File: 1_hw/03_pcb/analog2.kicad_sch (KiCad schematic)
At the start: 19 parts, among them U22 TPL0401B-10, U23 THS3491, U24 ADG1219BRJZ

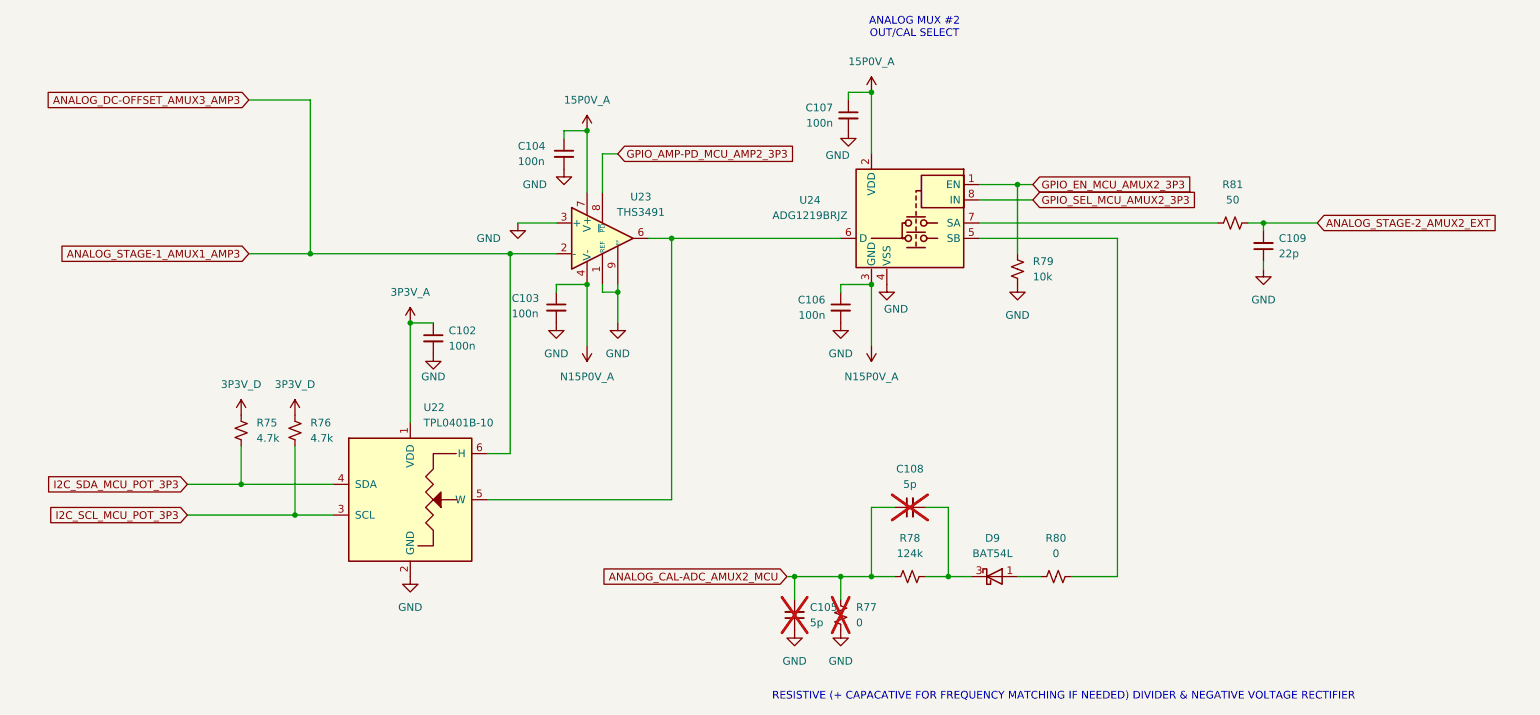
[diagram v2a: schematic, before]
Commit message: FEAT: Changed Inductor to higher current. Continued layout. Assigned some Netclasses.
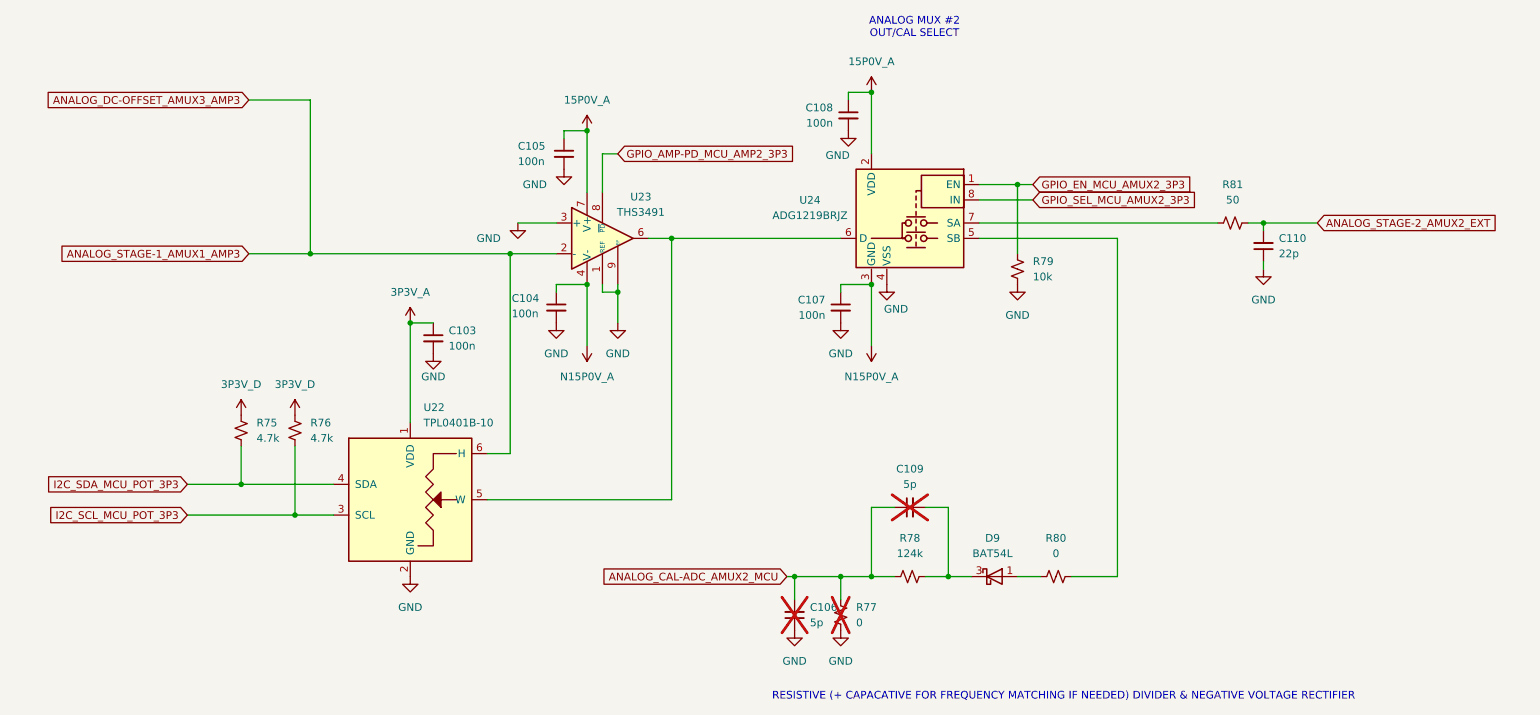
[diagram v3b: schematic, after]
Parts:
- renumbered C102 to C103, C103 to C104, C104 to C105, C105 to C106, C106 to C107, C107 to C108, C108 to C109, C109 to C110
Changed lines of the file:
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@@
 		(dnp no)
 		(fields_autoplaced yes)
-		(property "Reference" "#PWR0272"
+		(property "Reference" "#PWR0274"
 			(at 152.4 104.14 0)
 			(effects
@@
 			(project "arb"
 				(path "/866ef9be-3b01-4288-a6e0-a2357aa17e50/e46c6640-71a3-4b78-b602-0f6be9676e36"
-					(reference "#PWR0272")
+					(reference "#PWR0274")
 					(unit 1)
 				)
@@
 		(dnp no)
 		(fields_autoplaced yes)
-		(property "Reference" "#PWR0273"
+		(property "Reference" "#PWR0275"
 			(at 152.4 154.94 0)
 			(effects
@@
 			(project "arb"
 				(path "/866ef9be-3b01-4288-a6e0-a2357aa17e50/e46c6640-71a3-4b78-b602-0f6be9676e36"
-					(reference "#PWR0273")
+					(reference "#PWR0275")
 					(unit 1)
 				)
@@
 		(dnp no)
 		(fields_autoplaced yes)
-		(property "Reference" "#PWR0269"
+		(property "Reference" "#PWR0271"
 			(at 110.49 97.79 0)
 			(effects
@@
 			(project "arb"
 				(path "/866ef9be-3b01-4288-a6e0-a2357aa17e50/e46c6640-71a3-4b78-b602-0f6be9676e36"
-					(reference "#PWR0269")
+					(reference "#PWR0271")
 					(unit 1)
 				)
@@
 		(dnp no)
 		(fields_autoplaced yes)
-		(property "Reference" "C107"
+		(property "Reference" "C108"
 			(at 151.13 62.2363 0)
 			(effects
@@
 			(project "arb"
 				(path "/866ef9be-3b01-4288-a6e0-a2357aa17e50/e46c6640-71a3-4b78-b602-0f6be9676e36"
-					(reference "C107")
+					(reference "C108")
 					(unit 1)
 				)
@@
 		(dnp no)
 		(fields_autoplaced yes)
-		(property "Reference" "#PWR0271"
+		(property "Reference" "#PWR0273"
 			(at 144.78 154.94 0)
 			(effects
@@
 			(project "arb"
 				(path "/866ef9be-3b01-4288-a6e0-a2357aa17e50/e46c6640-71a3-4b78-b602-0f6be9676e36"
-					(reference "#PWR0271")
+					(reference "#PWR0273")
 					(unit 1)
 				)
@@
 		(on_board yes)
 		(dnp no)
-		(property "Reference" "#PWR0274"
+		(property "Reference" "#PWR0276"
 			(at 153.67 72.39 0)
 			(effects
@@
 			(project "arb"
 				(path "/866ef9be-3b01-4288-a6e0-a2357aa17e50/e46c6640-71a3-4b78-b602-0f6be9676e36"
-					(reference "#PWR0274")
+					(reference "#PWR0276")
 					(unit 1)
 				)
@@
 		(dnp yes)
 		(fields_autoplaced yes)
-		(property "Reference" "C105"
+		(property "Reference" "C106"
 			(at 147.32 144.7735 0)
 			(effects
@@
 			(project "arb"
 				(path "/866ef9be-3b01-4288-a6e0-a2357aa17e50/e46c6640-71a3-4b78-b602-0f6be9676e36"
-					(reference "C105")
+					(reference "C106")
 					(unit 1)
 				)
@@
 		(on_board yes)
 		(dnp no)
-		(property "Reference" "C104"
+		(property "Reference" "C105"
 			(at 99.06 68.58 0)
 			(effects
@@
 			(project "arb"
 				(path "/866ef9be-3b01-4288-a6e0-a2357aa17e50/e46c6640-71a3-4b78-b602-0f6be9676e36"
-					(reference "C104")
+					(reference "C105")
 					(unit 1)
 				)
@@
 		(dnp no)
 		(fields_autoplaced yes)
-		(property "Reference" "C106"
+		(property "Reference" "C107"
 			(at 149.86 93.9863 0)
 			(effects
@@
 			(project "arb"
 				(path "/866ef9be-3b01-4288-a6e0-a2357aa17e50/e46c6640-71a3-4b78-b602-0f6be9676e36"
-					(reference "C106")
+					(reference "C107")
 					(unit 1)
 				)
@@
 		(dnp no)
 		(fields_autoplaced yes)
-		(property "Reference" "#PWR0270"
+		(property "Reference" "#PWR0272"
 			(at 115.57 104.14 0)
 			(effects
@@
 			(project "arb"
 				(path "/866ef9be-3b01-4288-a6e0-a2357aa17e50/e46c6640-71a3-4b78-b602-0f6be9676e36"
-					(reference "#PWR0270")
+					(reference "#PWR0272")
 					(unit 1)
 				)
@@
 		(on_board yes)
 		(dnp no)
-		(property "Reference" "#PWR0267"
+		(property "Reference" "#PWR0269"
 			(at 106.68 78.74 0)
 			(effects
@@
 			(project "arb"
 				(path "/866ef9be-3b01-4288-a6e0-a2357aa17e50/e46c6640-71a3-4b78-b602-0f6be9676e36"
-					(reference "#PWR0267")
+					(reference "#PWR0269")
 					(unit 1)
 				)
@@
 		(on_board yes)
 		(dnp no)
-		(property "Reference" "C103"
+		(property "Reference" "C104"
 			(at 98.044 93.726 0)
 			(effects
@@
 			(project "arb"
 				(path "/866ef9be-3b01-4288-a6e0-a2357aa17e50/e46c6640-71a3-4b78-b602-0f6be9676e36"
-					(reference "C103")
+					(reference "C104")
 					(unit 1)
 				)
@@
 		(dnp no)
 		(fields_autoplaced yes)
-		(property "Reference" "#PWR0262"
+		(property "Reference" "#PWR0264"
 			(at 81.28 101.6 0)
 			(effects
@@
 			(project "arb"
 				(path "/866ef9be-3b01-4288-a6e0-a2357aa17e50/e46c6640-71a3-4b78-b602-0f6be9676e36"
-					(reference "#PWR0262")
+					(reference "#PWR0264")
 					(unit 1)
 				)
@@
 		(dnp no)
 		(fields_autoplaced yes)
-		(property "Reference" "#PWR0278"
+		(property "Reference" "#PWR0280"
 			(at 181.61 97.79 0)
 			(effects
@@
 			(project "arb"
 				(path "/866ef9be-3b01-4288-a6e0-a2357aa17e50/e46c6640-71a3-4b78-b602-0f6be9676e36"
-					(reference "#PWR0278")
+					(reference "#PWR0280")
 					(unit 1)
 				)
@@
 		(dnp no)
 		(fields_autoplaced yes)
-		(property "Reference" "#PWR0276"
+		(property "Reference" "#PWR0278"
 			(at 157.48 97.79 0)
 			(effects
@@
 			(project "arb"
 				(path "/866ef9be-3b01-4288-a6e0-a2357aa17e50/e46c6640-71a3-4b78-b602-0f6be9676e36"
-					(reference "#PWR0276")
+					(reference "#PWR0278")
 					(unit 1)
 				)
@@
 		(dnp no)
 		(fields_autoplaced yes)
-		(property "Reference" "#PWR0260"
+		(property "Reference" "#PWR0262"
 			(at 53.34 116.84 0)
 			(effects
@@
 			(project "arb"
 				(path "/866ef9be-3b01-4288-a6e0-a2357aa17e50/e46c6640-71a3-4b78-b602-0f6be9676e36"
-					(reference "#PWR0260")
+					(reference "#PWR0262")
 					(unit 1)
 				)
@@
 		(dnp yes)
 		(fields_autoplaced yes)
-		(property "Reference" "C108"
+		(property "Reference" "C109"
 			(at 163.8363 121.92 90)
 			(effects
@@
 			(project "arb"
 				(path "/866ef9be-3b01-4288-a6e0-a2357aa17e50/e46c6640-71a3-4b78-b602-0f6be9676e36"
-					(reference "C108")
+					(reference "C109")
 					(unit 1)
 				)
@@
 		(on_board yes)
 		(dnp no)
-		(property "Reference" "#PWR0277"
+		(property "Reference" "#PWR0279"
 			(at 160.02 97.79 0)
 			(effects
@@
 			(project "arb"
 				(path "/866ef9be-3b01-4288-a6e0-a2357aa17e50/e46c6640-71a3-4b78-b602-0f6be9676e36"
-					(reference "#PWR0277")
+					(reference "#PWR0279")
 					(unit 1)
 				)
@@
 		(dnp no)
 		(fields_autoplaced yes)
-		(property "Reference" "#PWR0266"
+		(property "Reference" "#PWR0268"
 			(at 105.41 104.14 0)
 			(effects
@@
 			(project "arb"
 				(path "/866ef9be-3b01-4288-a6e0-a2357aa17e50/e46c6640-71a3-4b78-b602-0f6be9676e36"
-					(reference "#PWR0266")
+					(reference "#PWR0268")
 					(unit 1)
 				)
@@
 		(dnp no)
 		(fields_autoplaced yes)
-		(property "Reference" "#PWR0261"
+		(property "Reference" "#PWR0263"
 			(at 62.23 116.84 0)
 			(effects
@@
 			(project "arb"
 				(path "/866ef9be-3b01-4288-a6e0-a2357aa17e50/e46c6640-71a3-4b78-b602-0f6be9676e36"
-					(reference "#PWR0261")
+					(reference "#PWR0263")
 					(unit 1)
 				)
@@
 		(dnp no)
 		(fields_autoplaced yes)
-		(property "Reference" "#PWR0263"
+		(property "Reference" "#PWR0265"
 			(at 81.28 146.05 0)
 			(effects
@@
 			(project "arb"
 				(path "/866ef9be-3b01-4288-a6e0-a2357aa17e50/e46c6640-71a3-4b78-b602-0f6be9676e36"
-					(reference "#PWR0263")
+					(reference "#PWR0265")
 					(unit 1)
 				)
@@
 		(dnp no)
 		(fields_autoplaced yes)
-		(property "Reference" "C102"
+		(property "Reference" "C103"
 			(at 87.63 99.0663 0)
 			(effects
@@
 			(project "arb"
 				(path "/866ef9be-3b01-4288-a6e0-a2357aa17e50/e46c6640-71a3-4b78-b602-0f6be9676e36"
-					(reference "C102")
+					(reference "C103")
 					(unit 1)
 				)
@@
 		(on_board yes)
 		(dnp no)
-		(property "Reference" "#PWR0264"
+		(property "Reference" "#PWR0266"
 			(at 85.09 109.22 0)
 			(effects
@@
 			(project "arb"
 				(path "/866ef9be-3b01-4288-a6e0-a2357aa17e50/e46c6640-71a3-4b78-b602-0f6be9676e36"
-					(reference "#PWR0264")
+					(reference "#PWR0266")
 					(unit 1)
 				)
@@
 		(dnp no)
 		(fields_autoplaced yes)
-		(property "Reference" "C109"
+		(property "Reference" "C110"
 			(at 224.79 83.8135 0)
 			(effects
@@
 			(project "arb"
 				(path "/866ef9be-3b01-4288-a6e0-a2357aa17e50/e46c6640-71a3-4b78-b602-0f6be9676e36"
-					(reference "C109")
+					(reference "C110")
 					(unit 1)
 				)
@@
 		(dnp no)
 		(fields_autoplaced yes)
-		(property "Reference" "#PWR0275"
+		(property "Reference" "#PWR0277"
 			(at 157.48 63.5 0)
 			(effects
@@
 			(project "arb"
 				(path "/866ef9be-3b01-4288-a6e0-a2357aa17e50/e46c6640-71a3-4b78-b602-0f6be9676e36"
-					(reference "#PWR0275")
+					(reference "#PWR0277")
 					(unit 1)
 				)
@@
 		(dnp no)
 		(fields_autoplaced yes)
-		(property "Reference" "#PWR0268"
+		(property "Reference" "#PWR0270"
 			(at 110.49 69.85 0)
 			(effects
@@
 			(project "arb"
 				(path "/866ef9be-3b01-4288-a6e0-a2357aa17e50/e46c6640-71a3-4b78-b602-0f6be9676e36"
-					(reference "#PWR0268")
+					(reference "#PWR0270")
 					(unit 1)
 				)
@@
 		(dnp no)
 		(fields_autoplaced yes)
-		(property "Reference" "#PWR0279"
+		(property "Reference" "#PWR0281"
 			(at 222.25 95.25 0)
 			(effects
@@
 			(project "arb"
 				(path "/866ef9be-3b01-4288-a6e0-a2357aa17e50/e46c6640-71a3-4b78-b602-0f6be9676e36"
-					(reference "#PWR0279")
+					(reference "#PWR0281")
 					(unit 1)
 				)
@@
 		(on_board yes)
 		(dnp no)
-		(property "Reference" "#PWR0265"
+		(property "Reference" "#PWR0267"
 			(at 99.06 87.63 0)
 			(effects
@@
 			(project "arb"
 				(path "/866ef9be-3b01-4288-a6e0-a2357aa17e50/e46c6640-71a3-4b78-b602-0f6be9676e36"
-					(reference "#PWR0265")
-					(unit 1)
-				)
+					(reference "#PWR0267")
+					(unit 1)
+				)
